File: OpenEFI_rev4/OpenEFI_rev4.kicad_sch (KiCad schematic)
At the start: 98 parts, among them J1 USB_B, J2 Tag connect, J4 Conn_02x08_Odd_Even, J7 Conn_01x04, J8 Micro_SD_Card_Det1, Q1 AO3400A, Q11 SS8050, Q12 AO3400A, Q19 AO3400A, Q2 AO3400A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

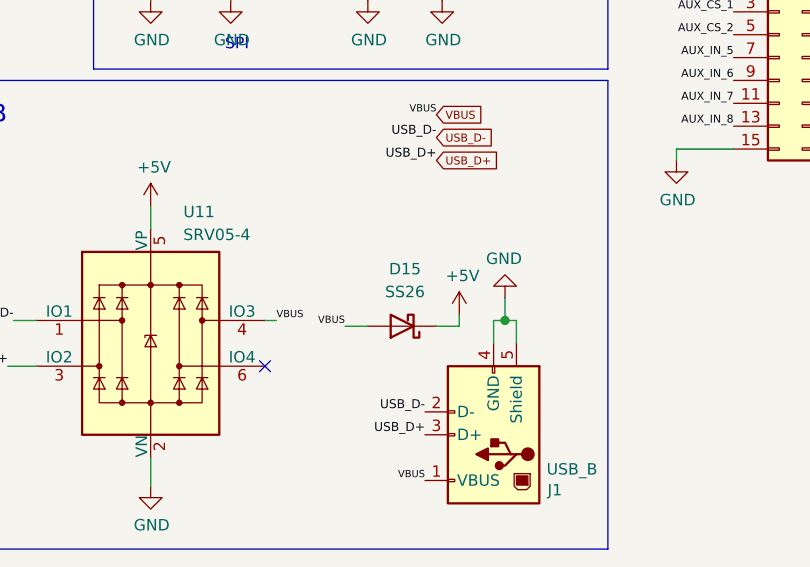
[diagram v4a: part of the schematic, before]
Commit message: add tacho driver
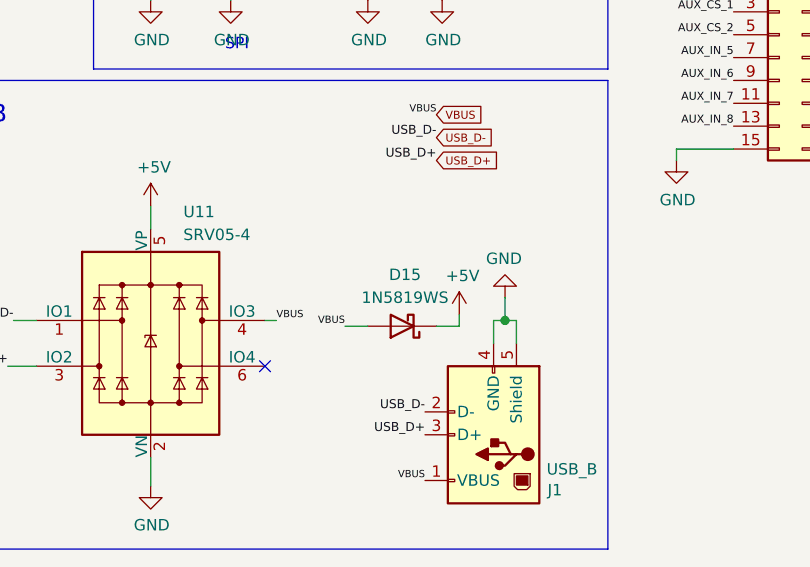
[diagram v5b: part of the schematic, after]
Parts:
- D15: value SS26 -> 1N5819WS; footprint Diode_SMD:D_SMA -> Diode_SMD:D_SOD-323_HandSoldering; LCSC C5350986 -> C191023
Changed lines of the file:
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@@
   (symbol (lib_id "Diode:SB160") (at 274.32 258.445 180) (unit 1)
     (in_bom yes) (on_board yes) (dnp no) (fields_autoplaced)
-    (property "Reference" "D15" (at 274.6375 252.095 0)
+    (property "Reference" "D15" (at 274.6375 252.73 0)
       (effects (font (size 1.27 1.27)))
     )
-    (property "Value" "SS26" (at 274.6375 254.635 0)
+    (property "Value" "1N5819WS" (at 274.6375 255.27 0)
       (effects (font (size 1.27 1.27)))
     )
-    (property "Footprint" "Diode_SMD:D_SMA" (at 274.32 254 0)
+    (property "Footprint" "Diode_SMD:D_SOD-323_HandSoldering" (at 274.32 254 0)
       (effects (font (size 1.27 1.27)) hide)
     )
@@
       (effects (font (size 1.27 1.27)) hide)
     )
-    (property "LCSC" "C5350986" (at 274.32 258.445 0)
+    (property "LCSC" "C191023" (at 274.32 258.445 0)
       (effects (font (size 0.889 0.889)) hide)
     )

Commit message: wip SD card
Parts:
- removed C12: 100nF, Capacitor_SMD:C_0805_2012Metric, symbol Device:C_Small
- removed J7: Conn_01x04, Connector_PinHeader_2.54mm:PinHeader_1x04_P2.54mm_Vertical, symbol Connector_Generic:Conn_01x04
- removed J8: Micro_SD_Card_Det1, Connector_Card:microSD_HC_Hirose_DM3AT-SF-PEJM5, symbol Connector:Micro_SD_Card_Det1
- added J3: 104031-0811, Library:MOLEX_104031-0811, symbol Library:104031-0811
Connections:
- net +3V3: now also RN6.8 (R1.2), J3.4 (VDD); no longer C5.1, C6.1
- net AUX_IN_6: now also U3.98 (PE1); no longer U3.92 (PB6)
- net GND: now also J3.6 (VSS), J3.9 (SW-1), J3.G1 (GND), J3.G2 (GND), J3.G3 (GND), J3.G4 (GND); no longer RN6.1 (R1.1), RN6.8 (R1.2)
- net MUX_A: now also U3.84 (PD3); no longer U3.83 (PD2)
- net MUX_B: now also U3.85 (PD4); no longer U3.84 (PD3)
- net MUX_C: now also U3.86 (PD5); no longer U3.85 (PD4)
- net SD_CD: now also U3.83 (PD2), J3.10 (SW-2); no longer U3.98 (PE1)
- net SD_CLK: now also RN6.4 (R4.1), J3.5 (CLK); no longer RN5.1 (R1.1)
- net SD_CMD: now also RN6.3 (R3.1), U3.92 (PB6), J3.3 (CMD); no longer RN5.2 (R2.1), U3.86 (PD5)
- net STEPPER_B2: no longer U23.11 (A2)
- net VDDA: now also C5.1, C6.1
- net A1 renamed TACHO_OUT
- net SD_DAT_0 renamed SD_DAT0
- net SD_DAT0: now also RN5.4 (R4.1), J3.7 (DAT0); no longer RN6.4 (R4.1)
- net SD_DAT_1 renamed SD_DAT1
- net SD_DAT1: now also RN5.3 (R3.1), J3.8 (DAT1); no longer RN6.3 (R3.1)
- net SD_DAT_2 renamed SD_DAT2
- net SD_DAT2: now also RN5.2 (R2.1), J3.1 (DAT2); no longer RN5.4 (R4.1)
- net SD_DAT_3 renamed SD_DAT3
- net SD_DAT3: now also RN5.1 (R1.1), J3.2 (CD/DAT3); no longer RN5.3 (R3.1)
- new net STEPPER_A2: U23.11 (A2)

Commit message: wip relay pcb
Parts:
- added TP39: TestPoint, TestPoint:TestPoint_Pad_1.0x1.0mm, symbol Connector:TestPoint
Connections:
- net SD_CMD: now also RN5.2 (R2.1); no longer RN6.3 (R3.1)
- net SD_DAT0: now also RN6.3 (R3.1); no longer RN5.4 (R4.1)
- net SD_DAT1: now also RN5.1 (R1.1); no longer RN5.3 (R3.1)
- net SD_DAT2: now also RN5.4 (R4.1); no longer RN5.2 (R2.1)
- net SD_DAT3: now also RN5.3 (R3.1); no longer RN5.1 (R1.1)
- net VDDA: now also TP39.1
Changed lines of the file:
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@@
     (stroke (width 0) (type solid))
   )
-  (wire (pts (xy 313.69 64.77) (xy 345.44 64.77))
-    (stroke (width 0) (type default))
-  )
   (wire (pts (xy 133.35 116.84) (xy 133.35 115.57))
     (stroke (width 0) (type solid))
@@
     (stroke (width 0) (type solid))
   )
-  (wire (pts (xy 318.77 52.07) (xy 345.44 52.07))
-    (stroke (width 0) (type default))
-  )
   (wire (pts (xy 397.51 110.49) (xy 401.32 110.49))
     (stroke (width 0) (type default))
@@
     (stroke (width 0.152) (type solid))
   )
+  (wire (pts (xy 342.9 64.77) (xy 345.44 64.77))
+    (stroke (width 0) (type default))
+  )
   (wire (pts (xy 69.85 45.085) (xy 75.565 45.085))
     (stroke (width 0) (type solid))
@@
     (stroke (width 0) (type solid))
   )
-  (wire (pts (xy 316.23 57.15) (xy 345.44 57.15))
-    (stroke (width 0) (type default))
-  )
   (wire (pts (xy 386.715 205.74) (xy 386.715 209.55))
     (stroke (width 0) (type solid))
@@
     (stroke (width 0) (type solid))
   )
-  (wire (pts (xy 318.77 39.37) (xy 318.77 52.07))
-    (stroke (width 0) (type default))
-  )
   (wire (pts (xy 25.4 130.175) (xy 25.4 127.635))
     (stroke (width 0) (type solid))
@@
     (stroke (width 0) (type solid))
   )
-  (wire (pts (xy 313.69 64.77) (xy 313.69 39.37))
-    (stroke (width 0) (type default))
-  )
   (wire (pts (xy 178.435 24.13) (xy 178.435 26.67))
     (stroke (width 0) (type default))
@@
     (stroke (width 0) (type solid))
   )
+  (wire (pts (xy 342.9 52.07) (xy 345.44 52.07))
+    (stroke (width 0) (type default))
+  )
   (wire (pts (xy 231.14 24.765) (xy 231.14 27.305))
     (stroke (width 0) (type default))
@@
     (stroke (width 0.152) (type solid))
   )
-  (wire (pts (xy 316.23 57.15) (xy 316.23 39.37))
-    (stroke (width 0) (type default))
-  )
   (wire (pts (xy 96.52 26.67) (xy 101.6 26.67))
     (stroke (width 0) (type solid))
@@
     (stroke (width 0.152) (type solid))
   )
+  (wire (pts (xy 342.9 57.15) (xy 345.44 57.15))
+    (stroke (width 0) (type default))
+  )
   (wire (pts (xy 190.5 171.45) (xy 193.04 171.45))
     (stroke (width 0) (type solid))
@@
     (effects (font (size 0.7874 0.7874)) (justify left bottom))
   )
-  (label "SD_CMD" (at 337.82 57.15 0) (fields_autoplaced)
-    (effects (font (size 0.7874 0.7874)) (justify left bottom))
+  (label "SD_CMD" (at 342.9 57.15 180) (fields_autoplaced)
+    (effects (font (size 0.7874 0.7874)) (justify right bottom))
   )
   (label "CAN1_TX" (at 142.24 194.31 180) (fields_autoplaced)
@@
     (effects (font (size 0.9906 0.9906)) (justify left bottom))
   )
+  (label "SD_CLK" (at 318.77 39.37 270) (fields_autoplaced)
+    (effects (font (size 0.7874 0.7874)) (justify right bottom))
+  )
   (label "CKP" (at 193.04 207.01 0) (fields_autoplaced)
     (effects (font (size 0.889 0.889)) (justify left bottom))
@@
     (effects (font (size 0.889 0.889)) (justify right bottom))
   )
-  (label "SD_DAT2" (at 328.93 38.1 270) (fields_autoplaced)
+  (label "SD_DAT2" (at 334.01 38.1 270) (fields_autoplaced)
     (effects (font (size 0.7874 0.7874)) (justify right bottom))
   )
@@
     (effects (font (size 0.8 0.8)) (justify left bottom))
   )
-  (label "SD_CD" (at 336.55 64.77 180) (fields_autoplaced)
+  (label "SD_CD" (at 342.9 64.77 180) (fields_autoplaced)
     (effects (font (size 0.889 0.889)) (justify right bottom))
   )
@@
     (effects (font (size 0.7874 0.7874)) (justify left bottom))
   )
-  (label "SD_DAT0" (at 334.01 38.1 270) (fields_autoplaced)
+  (label "SD_DAT0" (at 316.23 39.37 270) (fields_autoplaced)
     (effects (font (size 0.7874 0.7874)) (justify right bottom))
   )
@@
     (effects (font (size 0.7874 0.7874)) (justify left bottom))
   )
+  (label "SD_CMD" (at 328.93 38.1 270) (fields_autoplaced)
+    (effects (font (size 0.7874 0.7874)) (justify right bottom))
+  )
   (label "ADC_CS" (at 193.04 191.77 0) (fields_autoplaced)
     (effects (font (size 0.889 0.889)) (justify left bottom))
@@
     (effects (font (size 0.889 0.889)) (justify left bottom))
   )
-  (label "SD_DAT1" (at 331.47 38.1 270) (fields_autoplaced)
+  (label "SD_DAT1" (at 326.39 38.1 270) (fields_autoplaced)
     (effects (font (size 0.7874 0.7874)) (justify right bottom))
   )
@@
     (effects (font (size 0.889 0.889)) (justify right bottom))
   )
-  (label "SD_DAT3" (at 326.39 38.1 270) (fields_autoplaced)
+  (label "SD_DAT3" (at 331.47 38.1 270) (fields_autoplaced)
     (effects (font (size 0.7874 0.7874)) (justify right bottom))
   )
@@
     (effects (font (size 0.9906 0.9906)) (justify left bottom))
   )
+  (label "SD_CD" (at 313.69 39.37 270) (fields_autoplaced)
+    (effects (font (size 0.889 0.889)) (justify right bottom))
+  )
   (label "PMIC2_CS" (at 363.22 118.11 0) (fields_autoplaced)
     (effects (font (size 0.7874 0.7874)) (justify left bottom))
@@
         )
       )
+    )
+  )
+  (symbol (lib_id "Connector:TestPoint") (at 270.51 212.725 0) (unit 1)
+    (in_bom yes) (on_board yes) (dnp no)
+    (property "Reference" "TP39" (at 272.415 210.2484 0)
+      (effects (font (size 1.27 1.27)) (justify left))
+    )
+    (property "Value" "TestPoint" (at 272.415 212.7884 0)
+      (effects (font (size 1.27 1.27)) (justify left))
+    )
+    (property "Footprint" "TestPoint:TestPoint_Pad_1.0x1.0mm" (at 275.59 212.725 0)
+      (effects (font (size 1.27 1.27)) hide)
+    )
+    (property "Datasheet" "~" (at 275.59 212.725 0)
+      (effects (font (size 1.27 1.27)) hide)
+    )
+    (pin "1")
+    (instances
+      (project "OpenEFI_rev4"
+        (path "/b282ce4b-c3d0-4c94-b06c-73b92bb672a9"
+          (reference "TP39") (unit 1)
+        )
+      )

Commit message: WIP SPI
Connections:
- net CAN_RX is gone; now on net CAN1_RX: U25.4 (RXD)
- net CAN_TX is gone; now on net CAN1_TX: U25.1 (TXD)
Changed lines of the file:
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@@
     (effects (font (size 0.889 0.889)) (justify right bottom))
-  )
-  (label "USB_D+" (at 193.04 135.89 0) (fields_autoplaced)
-    (effects (font (size 0.9906 0.9906)) (justify left bottom))
   )
   (label "SD_CLK" (at 318.77 39.37 270) (fields_autoplaced)
@@
     (effects (font (size 0.8 0.8)) (justify right bottom))
   )
-  (label "CAN_RX" (at 22.225 250.19 0) (fields_autoplaced)
+  (label "CAN1_RX" (at 22.225 250.19 0) (fields_autoplaced)
     (effects (font (size 1.27 1.27)) (justify left bottom))
   )
   (label "LED_CAN_TX" (at 142.24 209.55 180) (fields_autoplaced)
     (effects (font (size 0.889 0.889)) (justify right bottom))
-  )
-  (label "USB_D+" (at 278.13 240.03 180) (fields_autoplaced)
-    (effects (font (size 0.9906 0.9906)) (justify right bottom))
   )
   (label "AUX_CS_2" (at 311.15 226.06 180) (fields_autoplaced)
@@
     (effects (font (size 0.7874 0.7874)) (justify left bottom))
   )
-  (label "VBUS" (at 278.13 234.95 180) (fields_autoplaced)
-    (effects (font (size 0.8 0.8)) (justify right bottom))
-  )
   (label "MEMORY_CS" (at 142.24 181.61 180) (fields_autoplaced)
     (effects (font (size 0.8 0.8)) (justify right bottom))
@@
     (effects (font (size 1.27 1.27)) (justify right bottom))
   )
-  (label "VBUS" (at 193.04 128.27 0) (fields_autoplaced)
-    (effects (font (size 0.8 0.8)) (justify left bottom))
-  )
   (label "CMP" (at 42.545 60.96 0) (fields_autoplaced)
     (effects (font (size 1.27 1.27)) (justify left bottom))
@@
     (effects (font (size 0.889 0.889)) (justify right bottom))
   )
-  (label "VBUS" (at 276.86 275.59 180) (fields_autoplaced)
-    (effects (font (size 0.8 0.8)) (justify right bottom))
-  )
   (label "AUX_IN_5" (at 193.04 161.29 0) (fields_autoplaced)
     (effects (font (size 0.889 0.889)) (justify left bottom))
@@
     (effects (font (size 1.27 1.27)) (justify right bottom))
   )
-  (label "USB_D-" (at 193.04 133.35 0) (fields_autoplaced)
-    (effects (font (size 0.9906 0.9906)) (justify left bottom))
-  )
   (label "RPM_OUT" (at 142.24 176.53 180) (fields_autoplaced)
     (effects (font (size 0.889 0.889)) (justify right bottom))
@@
   (label "MTR_DIR" (at 69.85 45.085 180) (fields_autoplaced)
     (effects (font (size 1.27 1.27)) (justify right bottom))
-  )
-  (label "USB_D-" (at 278.13 237.49 180) (fields_autoplaced)
-    (effects (font (size 0.9906 0.9906)) (justify right bottom))
   )
   (label "AUX_OUT_2" (at 193.04 204.47 0) (fields_autoplaced)
@@
     (effects (font (size 0.7874 0.7874)) (justify left bottom))
   )
-  (label "CAN_TX" (at 22.225 247.65 0) (fields_autoplaced)
+  (label "CAN1_TX" (at 22.225 247.65 0) (fields_autoplaced)
     (effects (font (size 1.27 1.27)) (justify left bottom))
   )
@@
     (effects (font (size 0.8 0.8)) (justify left bottom))
   )
-  (label "USB_D+" (at 276.86 270.51 180) (fields_autoplaced)
-    (effects (font (size 0.9906 0.9906)) (justify right bottom))
-  )
   (label "SYS_SWO" (at 40.005 76.835 0) (fields_autoplaced)
     (effects (font (size 0.9906 0.9906)) (justify left bottom))
@@
   (label "ECN2" (at 140.97 219.71 0) (fields_autoplaced)
     (effects (font (size 1.27 1.27)) (justify left bottom))
-  )
-  (label "USB_D-" (at 276.86 267.97 180) (fields_autoplaced)
-    (effects (font (size 0.9906 0.9906)) (justify right bottom))
   )
   (label "MIL_OUT" (at 194.31 125.73 0) (fields_autoplaced)
@@
     )
   )
-  (global_label "USB_D+" (shape input) (at 278.13 240.03 0) (fields_autoplaced)
-    (effects (font (size 0.889 0.889)) (justify left))
-    (property "Intersheetrefs" "${INTERSHEET_REFS}" (at 285.62 240.03 0)
-      (effects (font (size 1.27 1.27)) (justify left) hide)
+  (global_label "USB_D+" (shape input) (at 276.86 270.51 180) (fields_autoplaced)
+    (effects (font (size 0.889 0.889)) (justify right))
+    (property "Intersheetrefs" "${INTERSHEET_REFS}" (at 269.37 270.51 0)
+      (effects (font (size 1.27 1.27)) (justify right) hide)
     )
   )
@@
     )
   )
+  (global_label "VBUS" (shape input) (at 193.04 128.27 0) (fields_autoplaced)
+    (effects (font (size 0.889 0.889)) (justify left))
+    (property "Intersheetrefs" "${INTERSHEET_REFS}" (at 198.625 128.27 0)
+      (effects (font (size 1.27 1.27)) (justify left) hide)
+    )
+  )
   (global_label "ACC" (shape input) (at 205.74 274.32 0)
     (effects (font (size 0.889 0.889)) (justify left))
@@
     )
   )
+  (global_label "USB_D+" (shape input) (at 193.04 135.89 0) (fields_autoplaced)
+    (effects (font (size 0.889 0.889)) (justify left))
+    (property "Intersheetrefs" "${INTERSHEET_REFS}" (at 200.53 135.89 0)
+      (effects (font (size 1.27 1.27)) (justify left) hide)
+    )
+  )
+  (global_label "USB_D-" (shape input) (at 193.04 133.35 0) (fields_autoplaced)
+    (effects (font (size 0.889 0.889)) (justify left))
+    (property "Intersheetrefs" "${INTERSHEET_REFS}" (at 200.53 133.35 0)
+      (effects (font (size 1.27 1.27)) (justify left) hide)
+    )
+  )
   (global_label "CAN-" (shape input) (at 69.85 255.27 0)
     (effects (font (size 0.889 0.889)) (justify left))
@@
     )
   )
-  (global_label "USB_D-" (shape input) (at 278.13 237.49 0) (fields_autoplaced)
-    (effects (font (size 0.889 0.889)) (justify left))
-    (property "Intersheetrefs" "${INTERSHEET_REFS}" (at 285.62 237.49 0)
-      (effects (font (size 1.27 1.27)) (justify left) hide)
+  (global_label "USB_D-" (shape input) (at 276.86 267.97 180) (fields_autoplaced)
+    (effects (font (size 0.889 0.889)) (justify right))
+    (property "Intersheetrefs" "${INTERSHEET_REFS}" (at 269.37 267.97 0)
+      (effects (font (size 1.27 1.27)) (justify right) hide)
     )
   )
@@
     )
   )
-  (global_label "VBUS" (shape input) (at 278.13 234.95 0) (fields_autoplaced)
-    (effects (font (size 0.889 0.889)) (justify left))
-    (property "Intersheetrefs" "${INTERSHEET_REFS}" (at 283.715 234.95 0)
-      (effects (font (size 1.27 1.27)) (justify left) hide)
-    )
-  )
+  (global_label "VBUS" (shape input) (at 276.86 275.59 180) (fields_autoplaced)
+    (effects (font (size 0.889 0.889)) (justify right))
+    (property "Intersheetrefs" "${INTERSHEET_REFS}" (at 271.275 275.59 0)
+      (effects (font (size 1.27 1.27)) (justify right) hide)
+    )
+  )
